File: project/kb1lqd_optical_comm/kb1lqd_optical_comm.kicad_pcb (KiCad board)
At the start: 4 copper layers, 61 x 101.6 mm, 79 parts, among them J1 SJ1-3523N, J2 SJ-2509N, J3 SJ1-3523N, J4 Conn_01x04_Male, J5 Conn_01x02_Male, J6 SJ1-3523N, Q1 PMBF170, SW1 EG1213, SW2 EG1213, SW3 EG1213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

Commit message: More.
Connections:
- SW1 pad 1: /Michrophone Pre-Amp/AUDIO_OUTPUT -> /Headphone_Input/AUDIO_OUTPUT
- SW1 pad 3: /Headphone_Input/AUDIO_OUTPUT -> /Michrophone Pre-Amp/AUDIO_OUTPUT
- SW2 pad 1: /Photodiode Transimpedance Amplifier/OUTPUT -> Net-(J4-Pad2)
- SW2 pad 3: Net-(J4-Pad2) -> /Photodiode Transimpedance Amplifier/OUTPUT
- SW3 pad 1: Net-(J5-Pad2) -> Net-(D1-Pad2)
- SW3 pad 3: Net-(D1-Pad2) -> Net-(J5-Pad2)
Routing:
- net /LED Driver/AUDIO_INPUT: track 0.00 -> 31.8 mm
- net /Michrophone Pre-Amp/AUDIO_OUTPUT: track 7.14 -> 33.3 mm
- net /Headphone_Input/AUDIO_OUTPUT: track 0.00 -> 22.9 mm
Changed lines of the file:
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@@
     (thickness 1.6)
     (drawings 12)
-    (tracks 287)
+    (tracks 303)
     (zones 0)
     (modules 79)
@@
     (pad P$4 thru_hole circle (at -4.85 0 180) (size 2.25 2.25) (drill 1.5) (layers *.Cu *.Mask))
     (pad 3 thru_hole circle (at 2 0 180) (size 1.308 1.308) (drill 0.8) (layers *.Cu *.Mask)
-      (net 24 /Headphone_Input/AUDIO_OUTPUT))
-    (pad 1 thru_hole circle (at -2 0 180) (size 1.308 1.308) (drill 0.8) (layers *.Cu *.Mask)
       (net 27 "/Michrophone Pre-Amp/AUDIO_OUTPUT"))
+    (pad 1 thru_hole circle (at -2 0 180) (size 1.308 1.308) (drill 0.8) (layers *.Cu *.Mask)
+      (net 24 /Headphone_Input/AUDIO_OUTPUT))
     (pad 2 thru_hole circle (at 0 0 180) (size 1.308 1.308) (drill 0.8) (layers *.Cu *.Mask)
       (net 42 "/LED Driver/AUDIO_INPUT"))
@@
     (pad P$4 thru_hole circle (at -4.85 0 180) (size 2.25 2.25) (drill 1.5) (layers *.Cu *.Mask))
     (pad 3 thru_hole circle (at 2 0 180) (size 1.308 1.308) (drill 0.8) (layers *.Cu *.Mask)
-      (net 28 "Net-(D1-Pad2)"))
-    (pad 1 thru_hole circle (at -2 0 180) (size 1.308 1.308) (drill 0.8) (layers *.Cu *.Mask)
       (net 39 "Net-(J5-Pad2)"))
+    (pad 1 thru_hole circle (at -2 0 180) (size 1.308 1.308) (drill 0.8) (layers *.Cu *.Mask)
+      (net 28 "Net-(D1-Pad2)"))
     (pad 2 thru_hole circle (at 0 0 180) (size 1.308 1.308) (drill 0.8) (layers *.Cu *.Mask)
       (net 3 +5V))
@@
     (pad P$4 thru_hole circle (at -4.85 0) (size 2.25 2.25) (drill 1.5) (layers *.Cu *.Mask))
     (pad 3 thru_hole circle (at 2 0) (size 1.308 1.308) (drill 0.8) (layers *.Cu *.Mask)
-      (net 38 "Net-(J4-Pad2)"))
-    (pad 1 thru_hole circle (at -2 0) (size 1.308 1.308) (drill 0.8) (layers *.Cu *.Mask)
       (net 13 "/Photodiode Transimpedance Amplifier/OUTPUT"))
+    (pad 1 thru_hole circle (at -2 0) (size 1.308 1.308) (drill 0.8) (layers *.Cu *.Mask)
+      (net 38 "Net-(J4-Pad2)"))
     (pad 2 thru_hole circle (at 0 0) (size 1.308 1.308) (drill 0.8) (layers *.Cu *.Mask)
       (net 15 /Sheet5FD6A4A6/IN1))
@@
   (segment (start 152.845 109.855) (end 151.6634 109.855) (width 0.381) (layer F.Cu) (net 22))
   (segment (start 152.83 109.855) (end 151.6634 109.855) (width 0.381) (layer B.Cu) (net 22))
+  (segment (start 149.32 28.575) (end 149.32 35.0962) (width 0.381) (layer B.Cu) (net 24))
+  (segment (start 149.32 35.0962) (end 160.8836 46.6598) (width 0.381) (layer B.Cu) (net 24))
   (segment (start 145.359 50.047) (end 145.359 49.216) (width 0.254) (layer F.Cu) (net 25))
   (segment (start 145.359 49.216) (end 144.775 48.632) (width 0.254) (layer F.Cu) (net 25))
@@
   (segment (start 150.368 51.956) (end 150.368 53.218) (width 0.381) (layer F.Cu) (net 27))
   (segment (start 150.368 53.218) (end 150.375 53.225) (width 0.381) (layer F.Cu) (net 27))
-  (segment (start 150.375 53.225) (end 147.2 50.05) (width 0.381) (layer B.Cu) (net 27))
   (via (at 144.7 51.425) (size 0.5588) (drill 0.254) (layers F.Cu B.Cu) (net 27))
   (segment (start 144.709 50.047) (end 144.709 51.416) (width 0.254) (layer F.Cu) (net 27))
   (segment (start 144.709 51.416) (end 144.7 51.425) (width 0.254) (layer F.Cu) (net 27))
+  (segment (start 150.375 53.225) (end 150.375 52.1786) (width 0.381) (layer B.Cu) (net 27))
+  (segment (start 149.6214 51.425) (end 144.7 51.425) (width 0.381) (layer B.Cu) (net 27))
+  (segment (start 150.375 52.1786) (end 149.6214 51.425) (width 0.381) (layer B.Cu) (net 27))
+  (segment (start 145.32 28.575) (end 145.973999 29.228999) (width 0.381) (layer B.Cu) (net 27))
+  (segment (start 145.973999 29.228999) (end 145.973999 44.653395) (width 0.381) (layer B.Cu) (net 27))
+  (segment (start 144.7 50.372) (end 144.7 51.425) (width 0.381) (layer B.Cu) (net 27))
+  (segment (start 145.973999 44.653395) (end 145.2372 45.390194) (width 0.381) (layer B.Cu) (net 27))
+  (segment (start 145.2372 49.8348) (end 144.7 50.372) (width 0.381) (layer B.Cu) (net 27))
+  (segment (start 145.2372 45.390194) (end 145.2372 49.8348) (width 0.381) (layer B.Cu) (net 27))
   (segment (start 140.145 61.595) (end 136.8806 61.595) (width 0.381) (layer B.Cu) (net 30))
   (segment (start 136.8806 61.595) (end 136.6774 61.3918) (width 0.381) (layer B.Cu) (net 30))
@@
   (segment (start 163.7 56.5) (end 163.45 56.25) (width 0.381) (layer F.Cu) (net 41))
   (segment (start 163.45 56.25) (end 163.45 54.7) (width 0.381) (layer F.Cu) (net 41))
+  (segment (start 147.32 28.575) (end 147.32 41.148) (width 0.381) (layer F.Cu) (net 42))
+  (segment (start 147.32 41.148) (end 153.0096 46.8376) (width 0.381) (layer F.Cu) (net 42))
+  (segment (start 153.0096 46.8376) (end 153.0096 54.8386) (width 0.381) (layer F.Cu) (net 42))
+  (segment (start 153.0096 54.8386) (end 154.1526 55.9816) (width 0.381) (layer F.Cu) (net 42))
+  (segment (start 154.1526 55.9816) (end 155.6766 55.9816) (width 0.381) (layer F.Cu) (net 42))
+  (segment (start 155.6766 55.9816) (end 155.6766 56.007) (width 0.381) (layer F.Cu) (net 42))
   (segment (start 162.179 54.672) (end 162.179 56.304) (width 0.381) (layer F.Cu) (net 43))
   (segment (start 162.179 56.304) (end 162.325 56.45) (width 0.381) (layer F.Cu) (net 43))

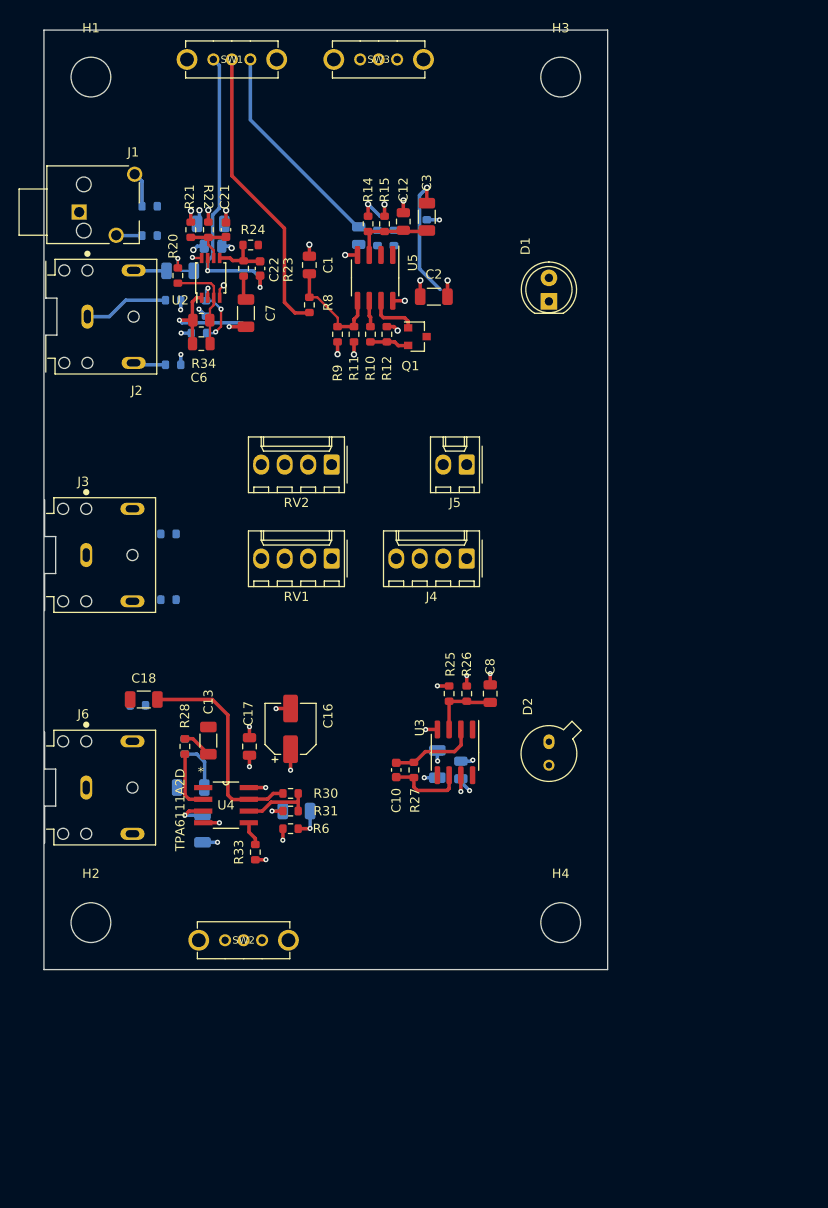
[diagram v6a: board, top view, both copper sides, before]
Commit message: Finished initial board. Downloaded audio jack footprint is causing errors on edge cut layer.
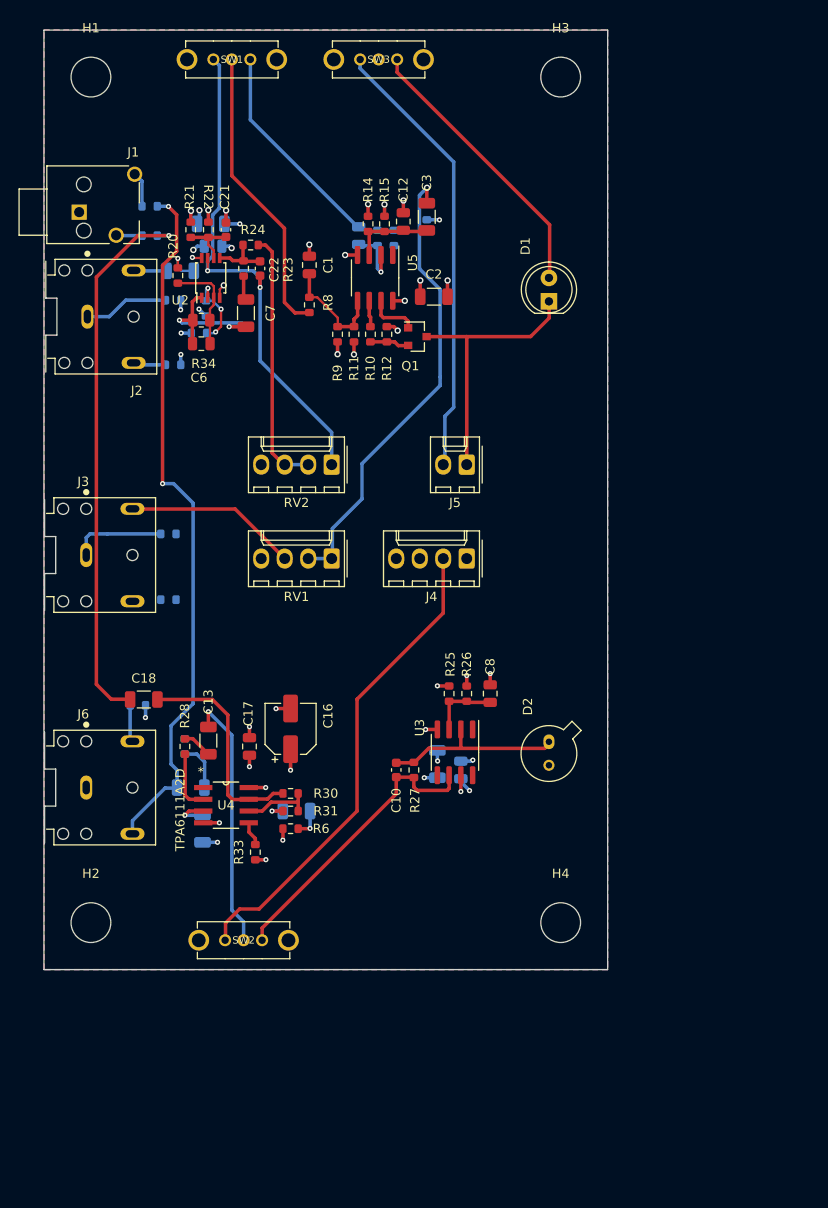
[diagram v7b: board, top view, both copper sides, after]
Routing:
- net AUDIO_OUT1: track 0.00 -> 76.3 mm, vias 0 -> 2
- net AUDIO_OUT2: track 0.00 -> 63.4 mm, vias 0 -> 1
- net Net-(J4-Pad2): track 0.00 -> 52.3 mm
- net Net-(J5-Pad2): track 0.00 -> 48.4 mm
- net Net-(C3-Pad2): track 13.9 -> 50.6 mm
- net Net-(D1-Pad2): track 0.00 -> 30.5 mm
- net /LED Driver/LED_RTN: track 0.00 -> 29.8 mm
- net Net-(R24-Pad1): track 0.00 -> 28.2 mm
- net /Sheet5FD6A4A6/IN1: track 0.00 -> 28.1 mm, vias 0 -> 1
- net /Photodiode Transimpedance Amplifier/OUTPUT: track 8.44 -> 32.2 mm
- net /Michrophone Pre-Amp/AUDIO_OUTPUT: track 33.3 -> 55.7 mm
- net /Headphone_Input/AUDIO_INPUT: track 0.00 -> 18.8 mm
- net Net-(C10-Pad2): track 9.43 -> 20.3 mm
- net Net-(J3-Pad1): track 0.00 -> 10.1 mm
- net Net-(C20-Pad2): track 0.00 -> 6.86 mm, vias 0 -> 1
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- added copper zone on B.Cu, net GND
- added copper zone on F.Cu, net GND

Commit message: No DRC errors.
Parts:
- R7: moved to F.Cu
- moved R7 3.17 mm to (137.2, 95.2)
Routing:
- net Net-(R28-Pad1): track 6.68 -> 13.5 mm, vias 0 -> 1
- net /Headphone_Input/AUDIO_OUTPUT: track 22.9 -> 26.8 mm
- net Net-(R17-Pad2): track 0.00 -> 3.44 mm, vias 0 -> 1
- net AUDIO_OUT2: track 63.4 -> 66.8 mm
- net Net-(C15-Pad1): track 5.23 -> 8.57 mm, vias 0 -> 1
- net Net-(J3-Pad2): track 0.00 -> 3.18 mm
- net GND: track 36.2 -> 37.6 mm, vias 27 -> 28
- net Net-(C6-Pad1): track 15.9 -> 14.7 mm
- net Net-(C3-Pad2): track 50.6 -> 51.5 mm
